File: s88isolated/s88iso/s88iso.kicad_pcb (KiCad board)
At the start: 2 copper layers, 70 x 50 mm, 33 parts, among them J1 Barrel_Jack_Switch_MountingPin, J2 5V Bypass, J3 12V 5V, J4 Conn_01x04, U1 LM317, U2 4504, U3 NSI8141W1

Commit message: modified ground a little bit
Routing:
- net GNDD: track 6.31 -> 9.34 mm, vias 6 -> 8

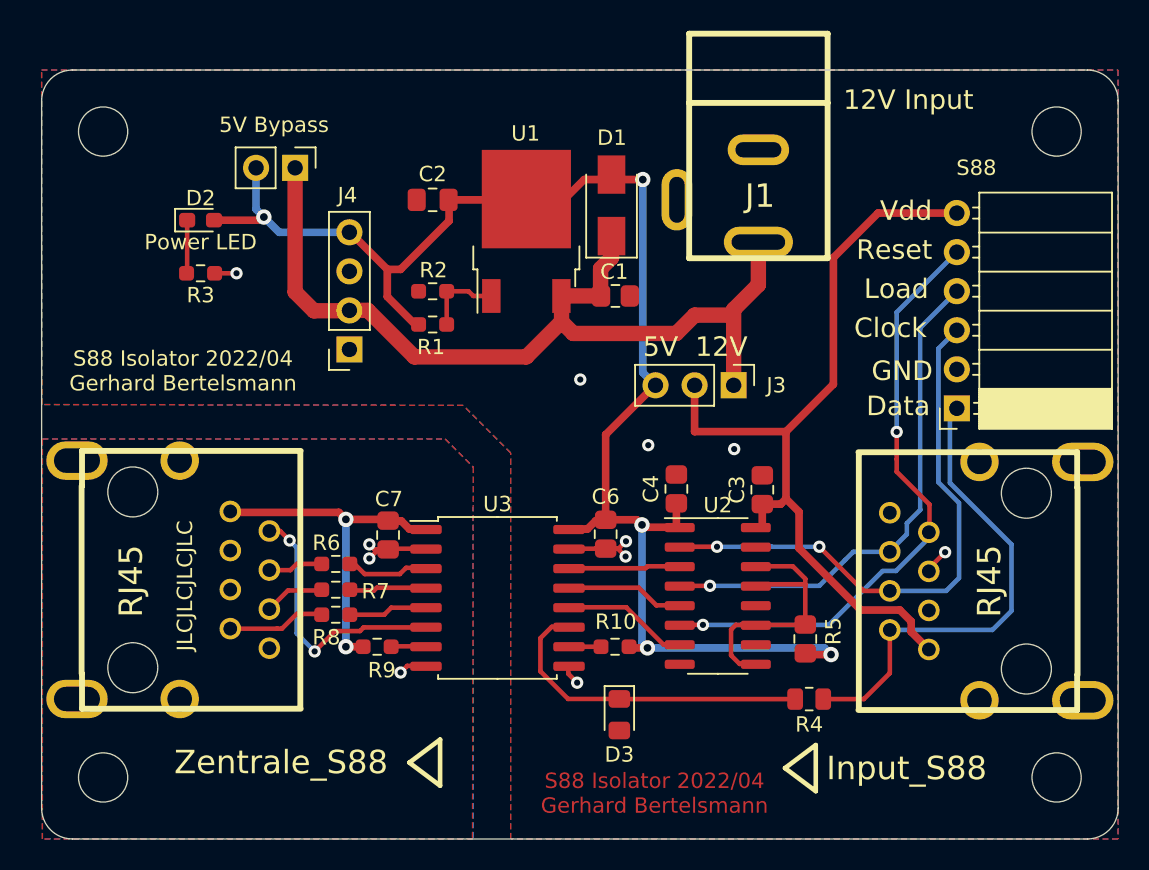
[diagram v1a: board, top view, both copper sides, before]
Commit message: change schematic to grid and LED JLCPCB
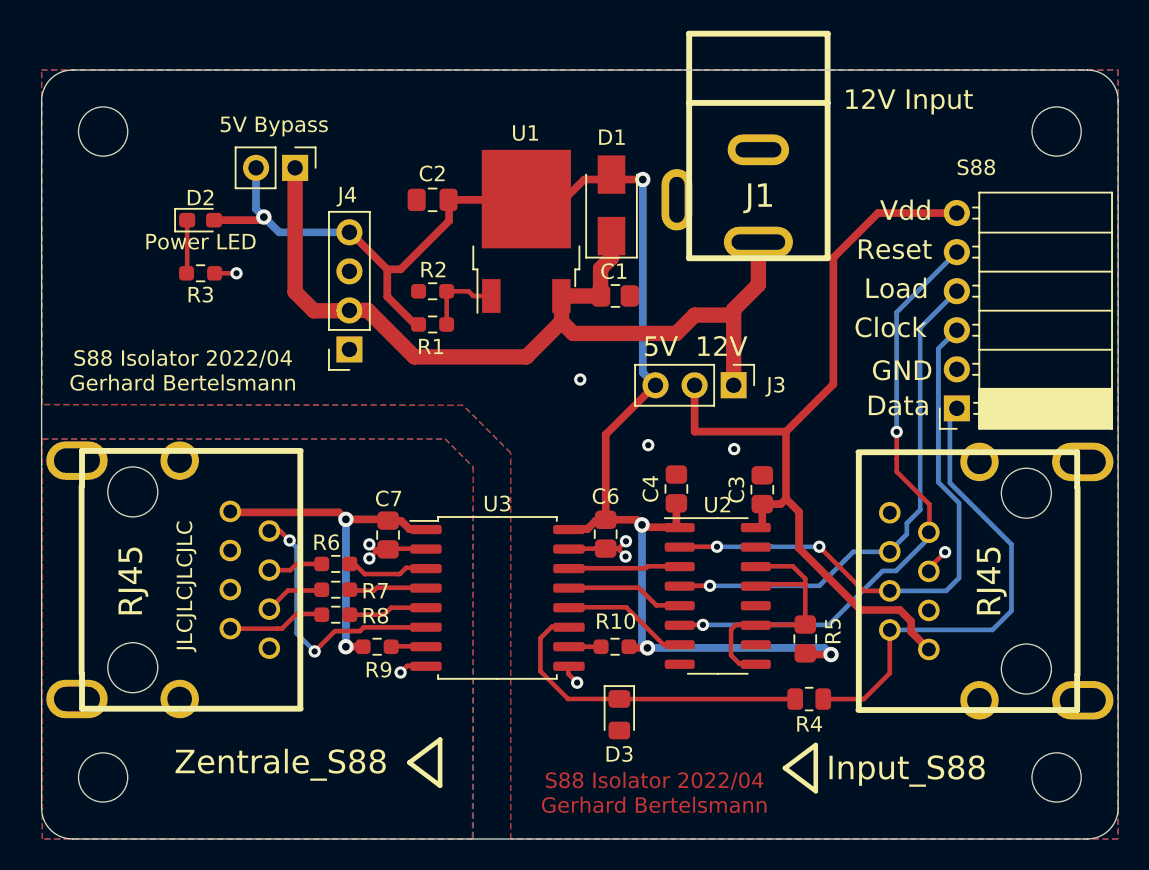
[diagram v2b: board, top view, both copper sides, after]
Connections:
- D1 pad 2: +5VD -> Net-(D1-A)
- Input_S88 pad 8: Net-(Input_S88-Pad8) -> unconnected-(Input_S88-Pad8)
- J2 pad 2: +5VD -> Net-(D1-A)
- J3 pad 3: +5VD -> Net-(D1-A)
- J4 pad 1: Net-(J4-Pad1) -> unconnected-(J4-Pin_1-Pad1)
- R1 pad 1: +5VD -> Net-(D1-A)
- U2 pad 10: Net-(U2-Pad10) -> unconnected-(U2-Dout-Pad10)
- U2 pad 12: Net-(U2-Pad12) -> unconnected-(U2-Eout-Pad12)
- U2 pad 15: Net-(U2-Pad15) -> unconnected-(U2-Fout-Pad15)
- Zentrale_S88 pad 8: Net-(Zentrale_S88-Pad8) -> unconnected-(Zentrale_S88-Pad8)
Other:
- net class Default removed
- net class Power removed
- net class Power2 removed
